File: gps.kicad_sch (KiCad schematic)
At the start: 7 parts, among them J3 5-1814832-2, U6 NEO-M9N

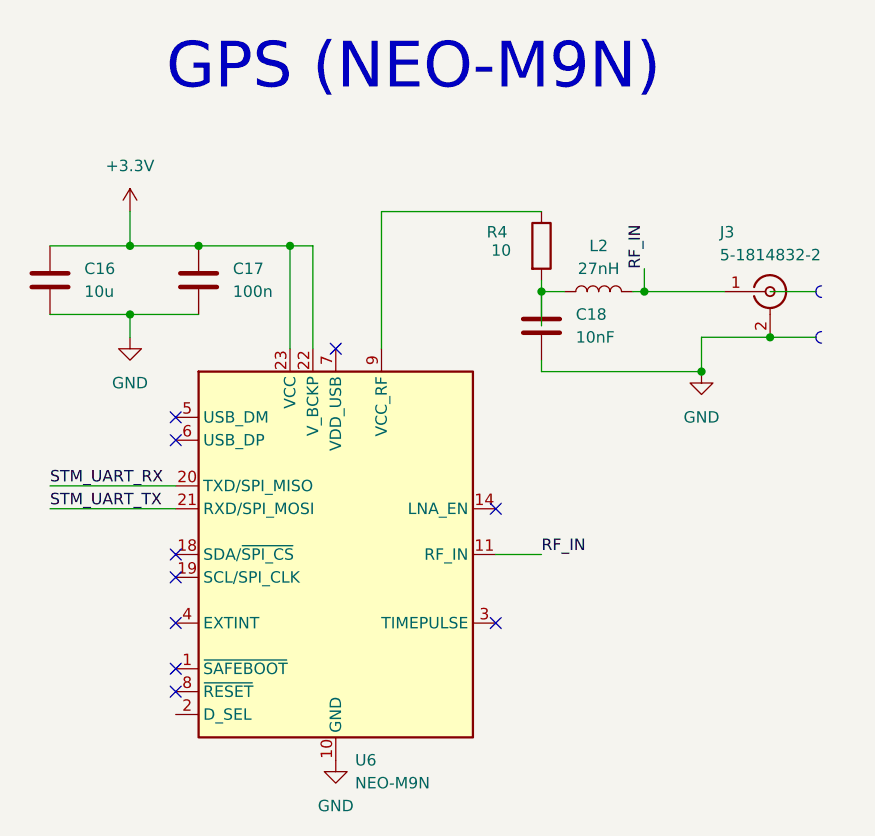
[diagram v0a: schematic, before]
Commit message: Fixed GPS, Radio, Baro, STM32, and added/rearanged some sheets (#26)
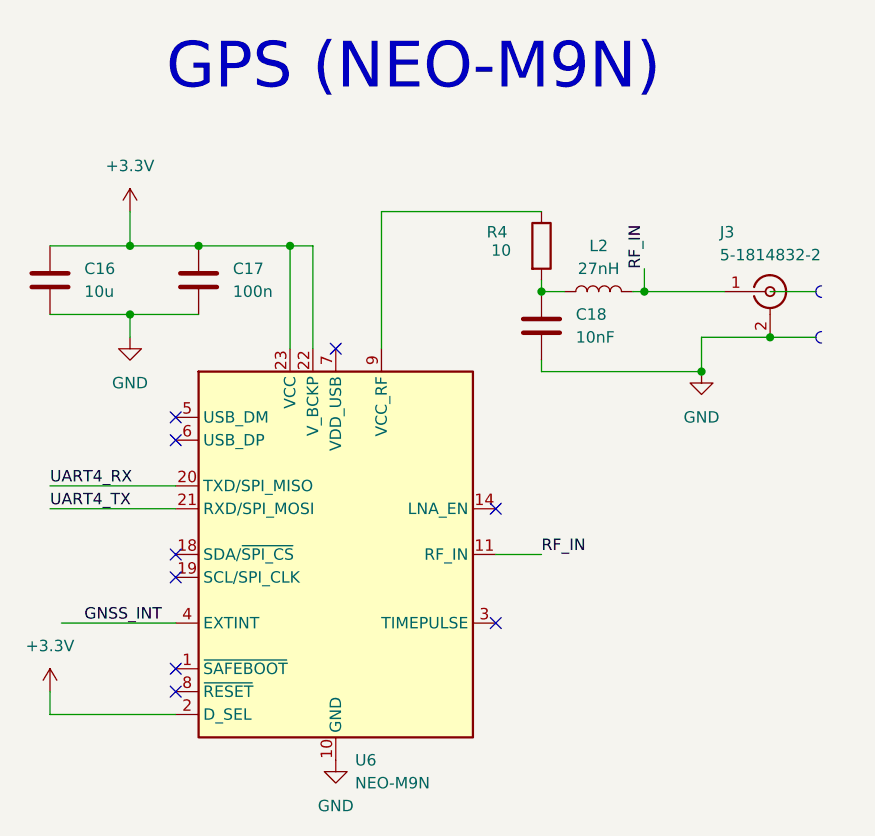
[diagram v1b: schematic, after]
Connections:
- net +3.3V: now also U6.2 (D_SEL)
- net GNSS_INT: now reaches U6.4 (EXTINT)
- net STM_UART_RX renamed UART4_RX
- net STM_UART_TX renamed UART4_TX
- no-connect marks 10 -> 9
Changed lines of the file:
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@@
+	)
+	(junction
+		(at 163.83 78.74)
+		(diameter 0)
+		(color 0 0 0 0)
 	)
 	(junction
@@
 	)
 	(junction
-		(at 189.23 83.82)
+		(at 181.61 87.63)
 		(diameter 0)
 		(color 0 0 0 0)
 	)
 	(junction
-		(at 181.61 87.63)
+		(at 189.23 83.82)
 		(diameter 0)
 		(color 0 0 0 0)
@@
 	)
 	(junction
-		(at 163.83 78.74)
-		(diameter 0)
-		(color 0 0 0 0)
-	)
-	(junction
 		(at 118.11 81.28)
 		(diameter 0)
@@
 	)
 	(no_connect
-		(at 123.19 115.57)
-	)
-	(no_connect
 		(at 140.97 85.09)
 	)
@@
 	(wire
 		(pts
+			(xy 109.22 125.73) (xy 123.19 125.73)
+		)
+		(stroke
+			(width 0)
+			(type default)
+		)
+	)
+	(wire
+		(pts
 			(xy 166.37 78.74) (xy 163.83 78.74)
 		)
@@
 	(wire
 		(pts
+			(xy 109.22 123.19) (xy 109.22 125.73)
+		)
+		(stroke
+			(width 0)
+			(type default)
+		)
+	)
+	(wire
+		(pts
 			(xy 118.11 81.28) (xy 125.73 81.28)
 		)
@@
 	(wire
 		(pts
+			(xy 163.83 86.36) (xy 163.83 87.63)
+		)
+		(stroke
+			(width 0)
+			(type default)
+		)
+	)
+	(wire
+		(pts
 			(xy 118.11 83.82) (xy 118.11 81.28)
 		)
@@
 	(wire
 		(pts
-			(xy 163.83 86.36) (xy 163.83 87.63)
-		)
-		(stroke
-			(width 0)
-			(type default)
-		)
-	)
-	(wire
-		(pts
 			(xy 118.11 73.66) (xy 125.73 73.66)
 		)
@@
 	(wire
 		(pts
-			(xy 163.83 78.74) (xy 163.83 82.55)
-		)
-		(stroke
-			(width 0)
-			(type default)
-		)
-	)
-	(wire
-		(pts
 			(xy 146.05 69.85) (xy 163.83 69.85)
 		)
@@
 	(wire
 		(pts
+			(xy 110.49 115.57) (xy 123.19 115.57)
+		)
+		(stroke
+			(width 0)
+			(type default)
+		)
+	)
+	(wire
+		(pts
 			(xy 118.11 69.85) (xy 118.11 73.66)
 		)
@@
 		)
 	)
-	(label "STM_UART_TX"
+	(label "UART4_RX"
+		(at 109.22 100.33 0)
+		(effects
+			(font
+				(size 1.27 1.27)
+			)
+			(justify left bottom)
+		)
+	)
+	(label "UART4_TX"
 		(at 109.22 102.87 0)
 		(effects
@@
 		)
 	)
-	(label "STM_UART_RX"
-		(at 109.22 100.33 0)
+	(label "RF_IN"
+		(at 175.26 76.2 90)
 		(effects
 			(font
@@
 		)
 	)
-	(label "RF_IN"
-		(at 175.26 76.2 90)
+	(label "GNSS_INT"
+		(at 113.03 115.57 0)
 		(effects
 			(font
@@
 	)
 	(symbol
+		(lib_id "power:+3.3V")
+		(at 109.22 123.19 0)
+		(unit 1)
+		(body_style 1)
+		(exclude_from_sim no)
+		(in_bom yes)
+		(on_board yes)
+		(in_pos_files yes)
+		(dnp no)
+		(fields_autoplaced yes)
+		(property "Reference" "#PWR029"
+			(at 109.22 127 0)
+			(hide yes)
+			(show_name no)
+			(do_not_autoplace no)
+			(effects
+				(font
+					(size 1.27 1.27)
+				)
+			)
+		)
+		(property "Value" "+3.3V"
+			(at 109.22 118.11 0)
+			(show_name no)
+			(do_not_autoplace no)
+			(effects
+				(font
+					(size 1.27 1.27)
+				)
+			)
+		)
+		(property "Footprint" ""
+			(at 109.22 123.19 0)
+			(hide yes)
+			(show_name no)
+			(do_not_autoplace no)
+			(effects
+				(font
+					(size 1.27 1.27)
+				)
+			)
+		)
+		(property "Datasheet" ""
+			(at 109.22 123.19 0)
+			(hide yes)
+			(show_name no)
+			(do_not_autoplace no)
+			(effects
+				(font
+					(size 1.27 1.27)
+				)
+			)
+		)
+		(property "Description" "Power symbol creates a global label with name \"+3.3V\""
+			(at 109.22 123.19 0)
+			(hide yes)
+			(show_name no)
+			(do_not_autoplace no)
+			(effects
+				(font
+					(size 1.27 1.27)
+				)
+			)
+		)
+		(pin "1"
+		)
+		(instances
+			(project "Control_Systems_PCB_2026-2027"
+				(path "/4cb8d8c9-28c6-4034-89a3-cec1725e3c68"
+					(reference "#PWR029")
+					(unit 1)
+				)
+			)
+		)
+	)
+	(symbol
 		(lib_id "RF_GPS:NEO-M9N")
 		(at 140.97 107.95 0)
@@
 		)
 	)
-	(embedded_fonts no)
 )
